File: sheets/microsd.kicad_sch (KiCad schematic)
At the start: 5 parts

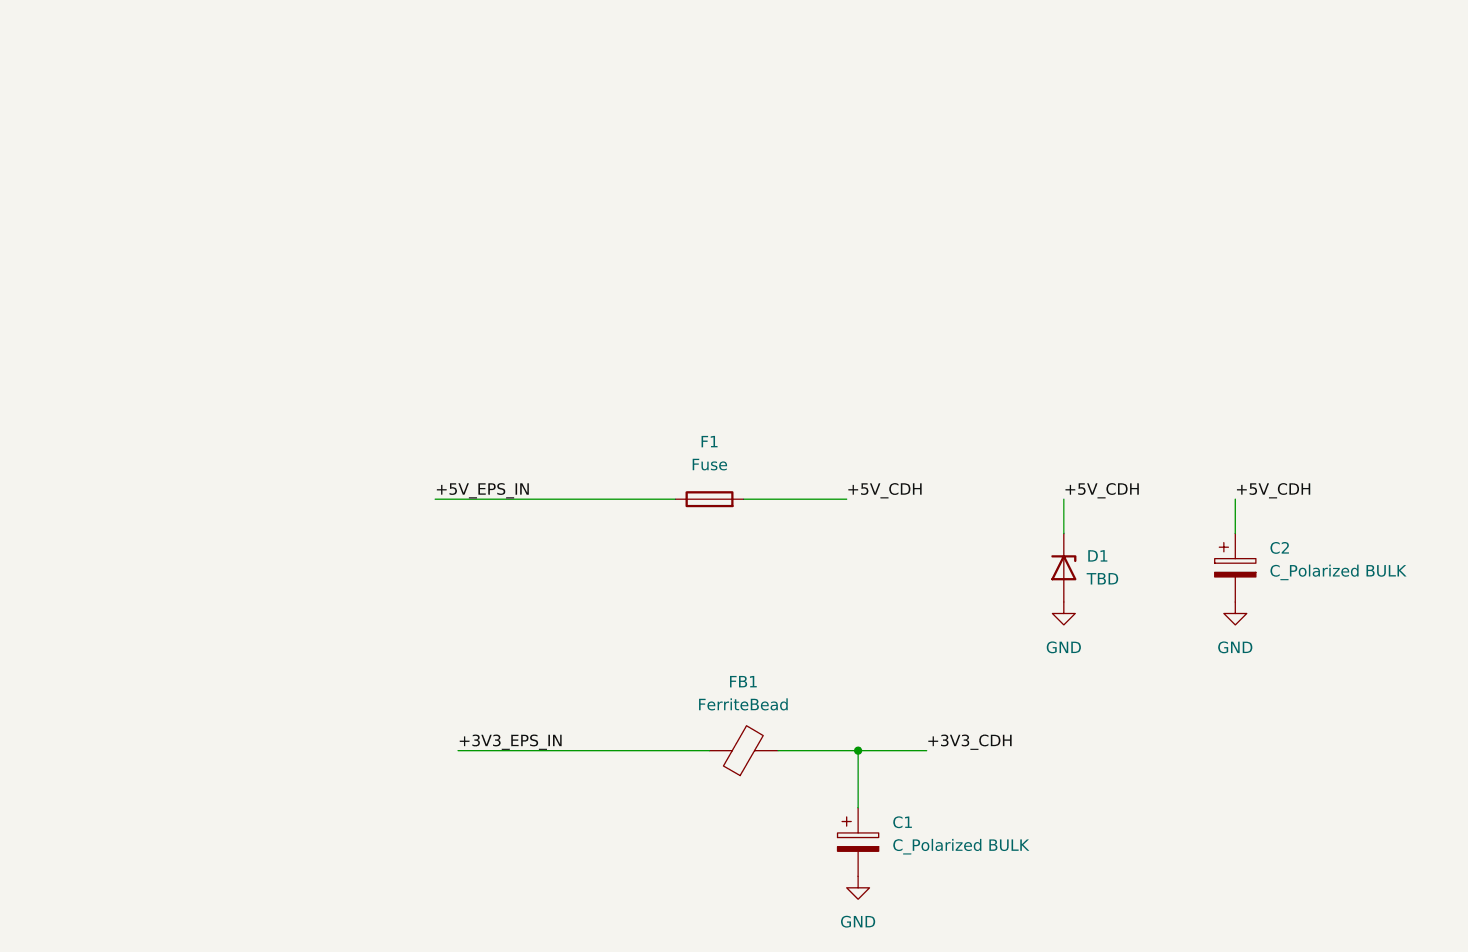
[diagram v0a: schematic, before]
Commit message: Payload USB updated to have 4 USB 2.0 Hub
Added support for USB flash or eUSB flash for storage.
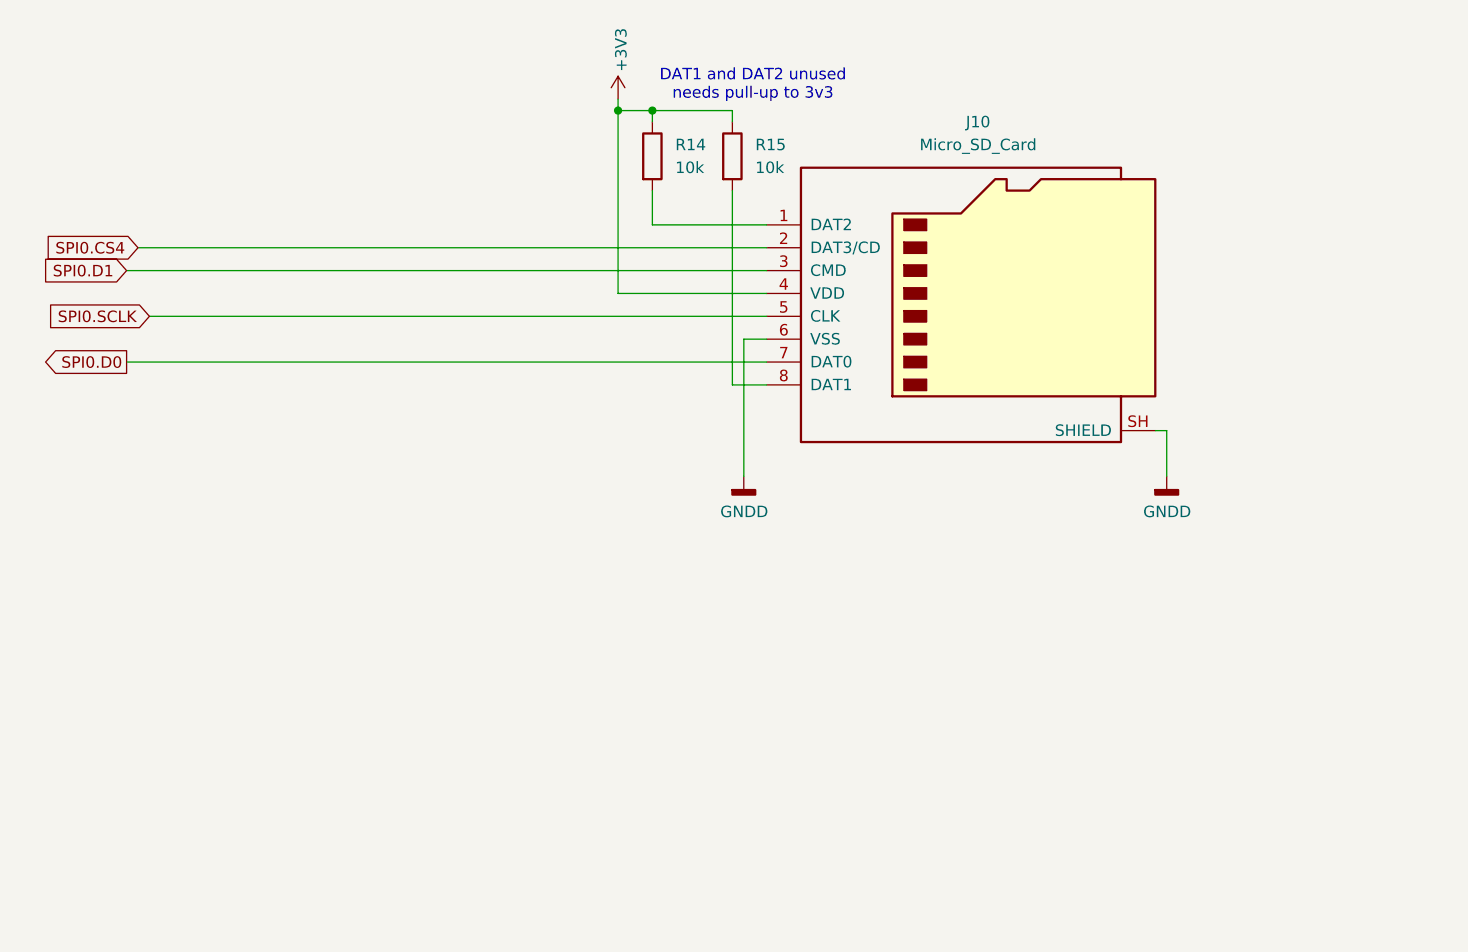
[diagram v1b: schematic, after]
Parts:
- removed C1, C2: C_Polarized BULK, symbol Device:C_Polarized
- removed D1: TBD, Diode_SMD:Nexperia_DSN1608-2_1.6x0.8mm, symbol Diode:PTVS5V0Z1USK
- removed F1: Fuse, symbol Device:Fuse
- removed FB1: FerriteBead, symbol Device:FerriteBead
- added J10: Micro_SD_Card, symbol Connector:Micro_SD_Card
- added R14, R15: 10k, symbol Device:R
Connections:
- new net: J10.1 (DAT2), R14.2
- new net: J10.8 (DAT1), R15.2
- new net +3V3: J10.4 (VDD), R14.1, R15.1
- new net GNDD: J10.6 (VSS), J10.SH (SHIELD)
- new net SPI0.CS4: J10.2 (DAT3/CD)
- new net SPI0.D0: J10.7 (DAT0)
- new net SPI0.D1: J10.3 (CMD)
- new net SPI0.SCLK: J10.5 (CLK)
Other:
- note added: "DAT1 and DAT2 unused needs pull-up to 3v3"
